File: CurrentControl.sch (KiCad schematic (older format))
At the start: 7 parts

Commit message: Initial Annotation
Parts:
- gave numbers to parts that had none: 7
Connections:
- net at R402.2: now also U201.7; no longer U201.1
- net at Q401.S, R403.1: now also U201.6 (-); no longer U201.2 (-)
- net at R401.1, RV401.3: now also U201.5 (+); no longer U201.3 (+)
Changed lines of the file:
@@
 $EndDescr
 $Comp
-L LMV358 U?
-U 1 1 54DADC5E
+L LMV358 U201
+U 2 1 54DADC5E
 P 5500 3700
-F 0 "U?" H 5450 3900 60  0000 L CNN
+F 0 "U201" H 5450 3900 60  0000 L CNN
 F 1 "LMV358" H 5450 3450 60  0000 L CNN
 F 2 "" H 5500 3700 60  0000 C CNN
 F 3 "" H 5500 3700 60  0000 C CNN
-	1    5500 3700
+	2    5500 3700
 	1    0    0    -1
 $EndComp
 $Comp
-L R R?
+L R R403
 U 1 1 54DADC66
 P 8100 5150
-F 0 "R?" V 8180 5150 50  0000 C CNN
+F 0 "R403" V 8180 5150 50  0000 C CNN
 F 1 ".1" V 8107 5151 50  0000 C CNN
 F 2 "" V 8030 5150 30  0000 C CNN
@@
 $EndComp
 $Comp
-L MOSFET_N Q?
+L MOSFET_N Q401
 U 1 1 54DADC74
 P 8000 3700
-F 0 "Q?" H 8010 3870 50  0000 R CNN
+F 0 "Q401" H 8010 3870 50  0000 R CNN
 F 1 "BUK9575" H 7950 3550 50  0000 R CNN
 F 2 "" H 8000 3700 60  0000 C CNN
@@
 $EndComp
 $Comp
-L R R?
+L R R401
 U 1 1 54DADC7B
 P 3600 4900
-F 0 "R?" V 3680 4900 50  0000 C CNN
+F 0 "R401" V 3680 4900 50  0000 C CNN
 F 1 "R" V 3607 4901 50  0000 C CNN
 F 2 "" V 3530 4900 30  0000 C CNN
@@
 $EndComp
 $Comp
-L GND #PWR?
+L GND #PWR402
 U 1 1 54DADC82
 P 5400 4250
-F 0 "#PWR?" H 5400 4000 60  0001 C CNN
+F 0 "#PWR402" H 5400 4000 60  0001 C CNN
 F 1 "GND" H 5400 4100 60  0000 C CNN
 F 2 "" H 5400 4250 60  0000 C CNN
@@
 Connection ~ 8100 5450
 $Comp
-L POT RV?
+L POT RV401
 U 1 1 54DADC9B
 P 3600 4200
-F 0 "RV?" H 3600 4100 50  0000 C CNN
+F 0 "RV401" H 3600 4100 50  0000 C CNN
 F 1 "POT" H 3600 4200 50  0000 C CNN
 F 2 "" H 3600 4200 60  0000 C CNN
@@
 Connection ~ 3750 2600
 $Comp
-L GND #PWR?
+L GND #PWR401
 U 1 1 54DADCA8
 P 4800 3300
-F 0 "#PWR?" H 4800 3050 60  0001 C CNN
+F 0 "#PWR401" H 4800 3050 60  0001 C CNN
 F 1 "GND" H 4800 3150 60  0000 C CNN
 F 2 "" H 4800 3300 60  0000 C CNN
@@
 $EndComp
 $Comp
-L C C?
+L C C401
 U 1 1 54DADCAE
 P 4800 3050
-F 0 "C?" H 4850 3150 50  0000 L CNN
+F 0 "C401" H 4850 3150 50  0000 L CNN
 F 1 "C" H 4850 2950 50  0000 L CNN
 F 2 "" H 4838 2900 30  0000 C CNN
@@
 	8650 1500 8100 1500
 $Comp
-L R R?
+L R R402
 U 1 1 54DAE31B
 P 6450 3700
-F 0 "R?" V 6530 3700 50  0000 C CNN
+F 0 "R402" V 6530 3700 50  0000 C CNN
 F 1 "1K" V 6457 3701 50  0000 C CNN
 F 2 "" V 6380 3700 30  0000 C CNN

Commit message: Preliminary association of components and placement into layout.
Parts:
- C401, R401, R402: footprint (none) -> SMD_Packages:SMD-0805
- Q401: footprint (none) -> Transistors_TO-220:TO-220_FET-GDS_Vertical
- R403: footprint (none) -> Resistors_ThroughHole:Resistor_Horizontal_RM15mm
- RV401: footprint (none) -> Potentiometers:Potentiometer_WirePads_largePads
- U201: footprint (none) -> SMD_Packages:SOIC-8-N
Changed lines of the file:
@@
 F 0 "U201" H 5450 3900 60  0000 L CNN
 F 1 "LMV358" H 5450 3450 60  0000 L CNN
-F 2 "" H 5500 3700 60  0000 C CNN
+F 2 "SMD_Packages:SOIC-8-N" H 5500 3700 60  0001 C CNN
 F 3 "" H 5500 3700 60  0000 C CNN
 	2    5500 3700
@@
 F 0 "R403" V 8180 5150 50  0000 C CNN
 F 1 ".1" V 8107 5151 50  0000 C CNN
-F 2 "" V 8030 5150 30  0000 C CNN
+F 2 "Resistors_ThroughHole:Resistor_Horizontal_RM15mm" V 8030 5150 30  0001 C CNN
 F 3 "" H 8100 5150 30  0000 C CNN
 F 4 "AC01000001007JA100" V 8100 5150 60  0001 C CNN "MPN"
@@
 F 0 "Q401" H 8010 3870 50  0000 R CNN
 F 1 "BUK9575" H 7950 3550 50  0000 R CNN
-F 2 "" H 8000 3700 60  0000 C CNN
+F 2 "Transistors_TO-220:TO-220_FET-GDS_Vertical" H 8000 3700 60  0001 C CNN
 F 3 "" H 8000 3700 60  0000 C CNN
 F 4 "BUK9575-100A,127" H 8000 3700 60  0001 C CNN "MPN"
@@
 F 0 "R401" V 3680 4900 50  0000 C CNN
 F 1 "R" V 3607 4901 50  0000 C CNN
-F 2 "" V 3530 4900 30  0000 C CNN
+F 2 "SMD_Packages:SMD-0805" V 3530 4900 30  0001 C CNN
 F 3 "" H 3600 4900 30  0000 C CNN
 	1    3600 4900
@@
 $EndComp
 $Comp
-L GND #PWR402
+L GND #PWR06
 U 1 1 54DADC82
 P 5400 4250
-F 0 "#PWR402" H 5400 4000 60  0001 C CNN
+F 0 "#PWR06" H 5400 4000 60  0001 C CNN
 F 1 "GND" H 5400 4100 60  0000 C CNN
 F 2 "" H 5400 4250 60  0000 C CNN
@@
 F 0 "RV401" H 3600 4100 50  0000 C CNN
 F 1 "POT" H 3600 4200 50  0000 C CNN
-F 2 "" H 3600 4200 60  0000 C CNN
+F 2 "Potentiometers:Potentiometer_WirePads_largePads" H 3600 4200 60  0001 C CNN
 F 3 "" H 3600 4200 60  0000 C CNN
 	1    3600 4200
@@
 Connection ~ 3750 2600
 $Comp
-L GND #PWR401
+L GND #PWR07
 U 1 1 54DADCA8
 P 4800 3300
-F 0 "#PWR401" H 4800 3050 60  0001 C CNN
+F 0 "#PWR07" H 4800 3050 60  0001 C CNN
 F 1 "GND" H 4800 3150 60  0000 C CNN
 F 2 "" H 4800 3300 60  0000 C CNN
@@
 F 0 "C401" H 4850 3150 50  0000 L CNN
 F 1 "C" H 4850 2950 50  0000 L CNN
-F 2 "" H 4838 2900 30  0000 C CNN
+F 2 "SMD_Packages:SMD-0805" H 4838 2900 30  0001 C CNN
 F 3 "" H 4800 3050 60  0000 C CNN
 	1    4800 3050
@@
 F 0 "R402" V 6530 3700 50  0000 C CNN
 F 1 "1K" V 6457 3701 50  0000 C CNN
-F 2 "" V 6380 3700 30  0000 C CNN
+F 2 "SMD_Packages:SMD-0805" V 6380 3700 30  0001 C CNN
 F 3 "" H 6450 3700 30  0000 C CNN
 	1    6450 3700

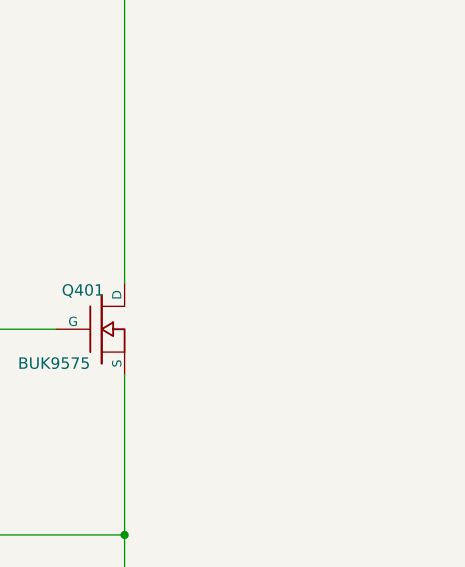
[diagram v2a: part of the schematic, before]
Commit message: Created new footprint library and created a heatsink footprint.
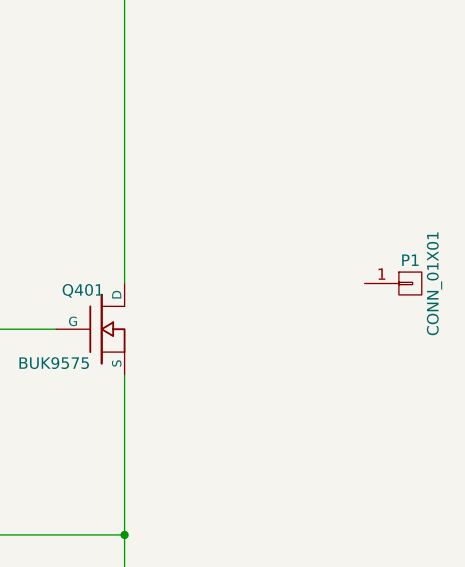
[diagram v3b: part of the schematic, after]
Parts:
- added P1: CONN_01X01, symbol CONN_01X01
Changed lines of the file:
@@
 Text HLabel 8550 6000 2    60   Input ~ 0
 Current_Sink-
+$Comp
+L CONN_01X01 P1
+U 1 1 54DFC527
+P 9350 3500
+F 0 "P1" H 9350 3600 50  0000 C CNN
+F 1 "CONN_01X01" V 9450 3500 50  0000 C CNN
+F 2 "" H 9350 3500 60  0000 C CNN
+F 3 "" H 9350 3500 60  0000 C CNN
+	1    9350 3500
+	1    0    0    -1
+$EndComp
 $EndSCHEMATC

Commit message: Added new potentiometer footprints to layout
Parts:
- P1: footprint (none) -> Current:FA-T220-38E
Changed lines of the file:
@@
 F 0 "P1" H 9350 3600 50  0000 C CNN
 F 1 "CONN_01X01" V 9450 3500 50  0000 C CNN
-F 2 "" H 9350 3500 60  0000 C CNN
+F 2 "Current:FA-T220-38E" H 9350 3500 60  0001 C CNN
 F 3 "" H 9350 3500 60  0000 C CNN
 	1    9350 3500

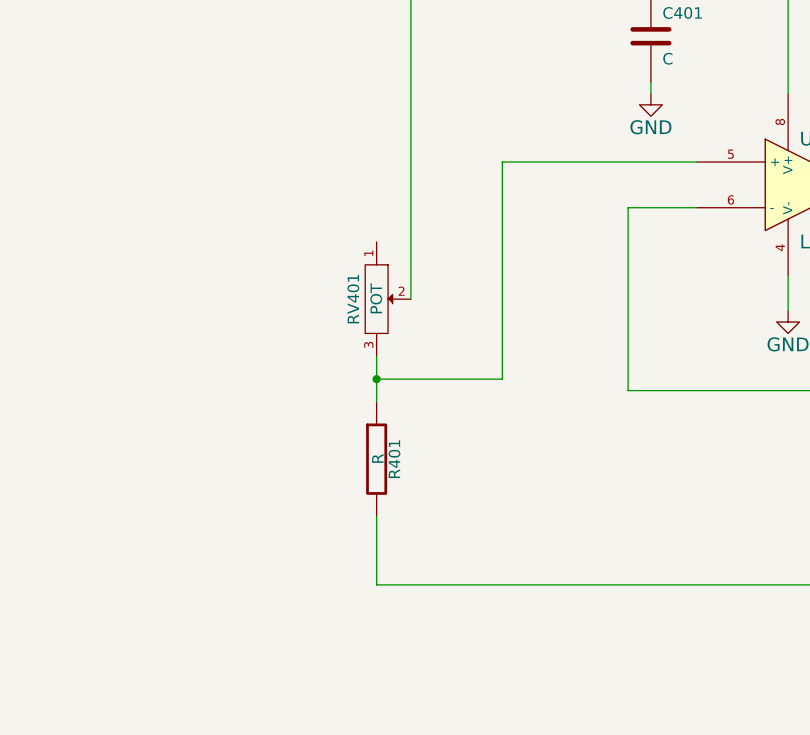
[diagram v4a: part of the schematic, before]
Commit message: Fixed divider resistors and found values
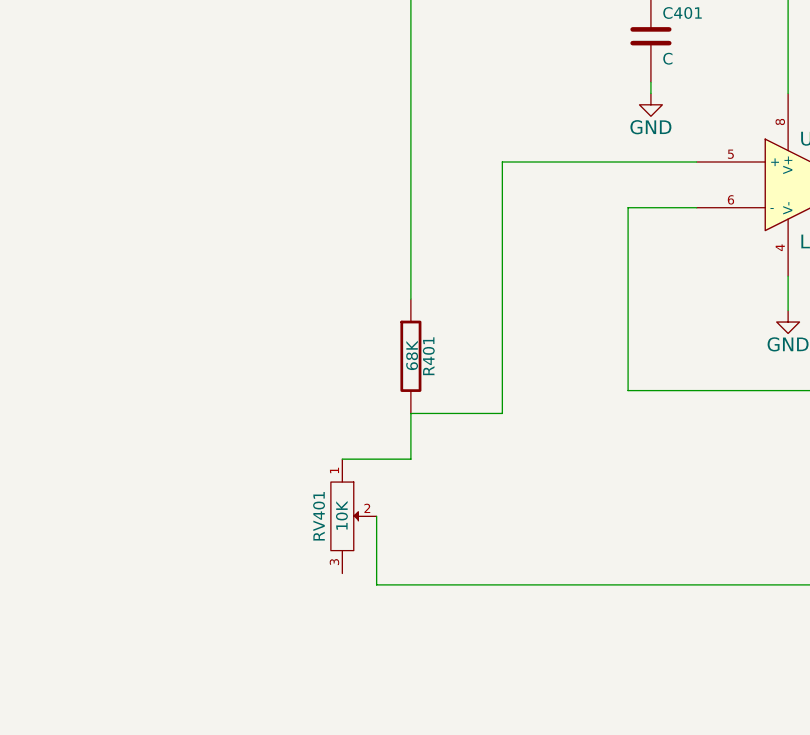
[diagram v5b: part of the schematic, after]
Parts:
- R401: value R -> 68K
- RV401: value POT -> 10K; footprint Potentiometers:Potentiometer_WirePads_largePads -> Current:P090L-02F25BR10K; MPN (none) -> P090L-02F25BR10K
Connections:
- net 2.7V: now also R401.1; no longer RV401.2
- net Current_Sink-: now also RV401.2; no longer R401.2
- net at RV401.1: now also R401.2, U201.5 (+)
- now unconnected: RV401.3
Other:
- moved on the sheet: R401, RV401
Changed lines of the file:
@@
 L R R401
 U 1 1 54DADC7B
-P 3600 4900
-F 0 "R401" V 3680 4900 50  0000 C CNN
-F 1 "R" V 3607 4901 50  0000 C CNN
-F 2 "SMD_Packages:SMD-0805" V 3530 4900 30  0001 C CNN
-F 3 "" H 3600 4900 30  0000 C CNN
-	1    3600 4900
+P 3750 4450
+F 0 "R401" V 3830 4450 50  0000 C CNN
+F 1 "68K" V 3757 4451 50  0000 C CNN
+F 2 "SMD_Packages:SMD-0805" V 3680 4450 30  0001 C CNN
+F 3 "" H 3750 4450 30  0000 C CNN
+	1    3750 4450
 	1    0    0    -1
 $EndComp
@@
 	5000 3600 4150 3600
 Wire Wire Line
-	4150 3600 4150 4550
-Wire Wire Line
-	4150 4550 3600 4550
-Wire Wire Line
-	3600 4450 3600 4650
-Connection ~ 3600 4550
+	4150 3600 4150 4700
 Wire Wire Line
 	3600 5150 3600 5450
@@
 L POT RV401
 U 1 1 54DADC9B
-P 3600 4200
-F 0 "RV401" H 3600 4100 50  0000 C CNN
-F 1 "POT" H 3600 4200 50  0000 C CNN
-F 2 "Potentiometers:Potentiometer_WirePads_largePads" H 3600 4200 60  0001 C CNN
-F 3 "" H 3600 4200 60  0000 C CNN
-	1    3600 4200
+P 3450 5150
+F 0 "RV401" H 3450 5050 50  0000 C CNN
+F 1 "10K" H 3450 5150 50  0000 C CNN
+F 2 "Current:P090L-02F25BR10K" H 3450 5150 60  0001 C CNN
+F 3 "" H 3450 5150 60  0000 C CNN
+F 4 "P090L-02F25BR10K" H 3450 5150 60  0001 C CNN "MPN"
+	1    3450 5150
 	0    1    1    0
 $EndComp
@@
 	1    0    0    -1
 $EndComp
+Wire Wire Line
+	4150 4700 3750 4700
+Wire Wire Line
+	3750 4700 3750 4900
+Wire Wire Line
+	3750 4900 3450 4900
 $EndSCHEMATC

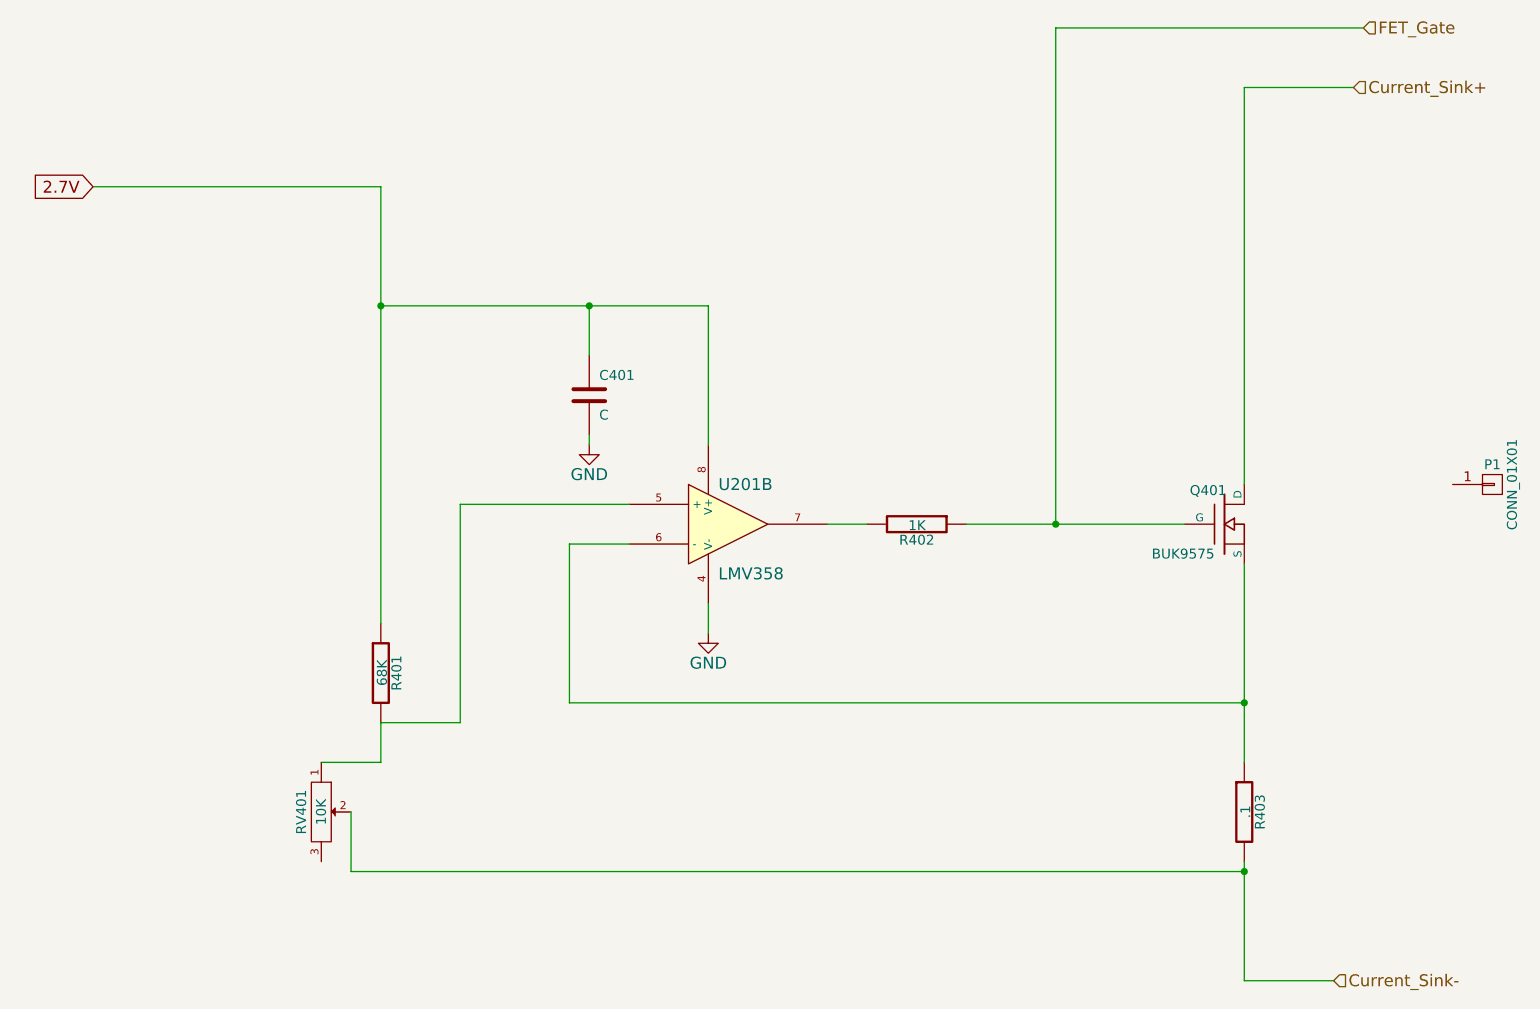
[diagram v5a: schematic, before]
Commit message: Cosmetic cleanup of schematic
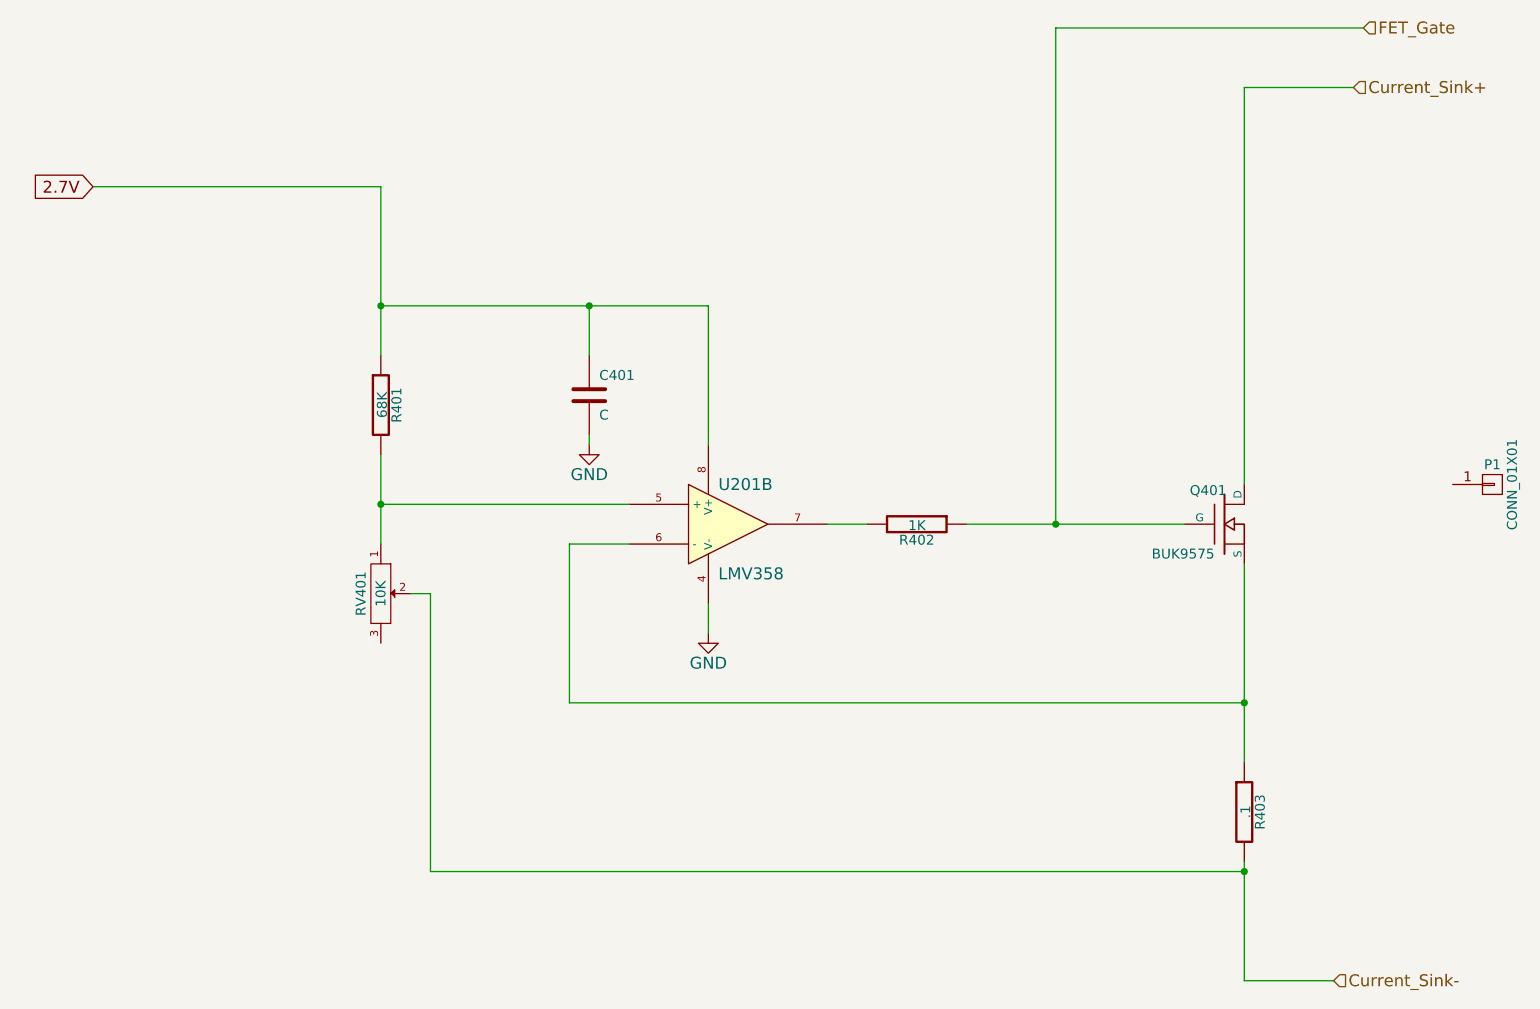
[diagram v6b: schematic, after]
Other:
- moved on the sheet: R401, RV401
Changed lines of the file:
@@
-$EndComp
-$Comp
-L R R401
-U 1 1 54DADC7B
-P 3750 4450
-F 0 "R401" V 3830 4450 50  0000 C CNN
-F 1 "68K" V 3757 4451 50  0000 C CNN
-F 2 "SMD_Packages:SMD-0805" V 3680 4450 30  0001 C CNN
-F 3 "" H 3750 4450 30  0000 C CNN
-	1    3750 4450
-	1    0    0    -1
 $EndComp
 $Comp
@@
 Connection ~ 8100 4600
 Wire Wire Line
-	5000 3600 4150 3600
-Wire Wire Line
-	4150 3600 4150 4700
-Wire Wire Line
-	3600 5150 3600 5450
-Wire Wire Line
-	3600 5450 8100 5450
+	3750 3600 5000 3600
 Connection ~ 8100 5450
 $Comp
 L POT RV401
 U 1 1 54DADC9B
-P 3450 5150
-F 0 "RV401" H 3450 5050 50  0000 C CNN
-F 1 "10K" H 3450 5150 50  0000 C CNN
-F 2 "Current:P090L-02F25BR10K" H 3450 5150 60  0001 C CNN
-F 3 "" H 3450 5150 60  0000 C CNN
-F 4 "P090L-02F25BR10K" H 3450 5150 60  0001 C CNN "MPN"
-	1    3450 5150
+P 3750 4050
+F 0 "RV401" H 3750 3950 50  0000 C CNN
+F 1 "10K" H 3750 4050 50  0000 C CNN
+F 2 "Current:P090L-02F25BR10K" H 3750 4050 60  0001 C CNN
+F 3 "" H 3750 4050 60  0000 C CNN
+F 4 "P090L-02F25BR10K" H 3750 4050 60  0001 C CNN "MPN"
+	1    3750 4050
 	0    1    1    0
 $EndComp
@@
 	2300 2000 3750 2000
 Wire Wire Line
-	3750 2000 3750 4200
+	3750 2000 3750 2850
 Text HLabel 8650 1500 2    60   Input ~ 0
 Current_Sink+
@@
 	1    0    0    -1
 $EndComp
+$Comp
+L R R401
+U 1 1 54DADC7B
+P 3750 3100
+F 0 "R401" V 3830 3100 50  0000 C CNN
+F 1 "68K" V 3757 3101 50  0000 C CNN
+F 2 "SMD_Packages:SMD-0805" V 3680 3100 30  0001 C CNN
+F 3 "" H 3750 3100 30  0000 C CNN
+	1    3750 3100
+	1    0    0    -1
+$EndComp
 Wire Wire Line
-	4150 4700 3750 4700
+	3750 3350 3750 3800
+Connection ~ 3750 3600
 Wire Wire Line
-	3750 4700 3750 4900
+	3900 4050 4000 4050
 Wire Wire Line
-	3750 4900 3450 4900
+	4000 4050 4000 5450
+Wire Wire Line
+	4000 5450 8100 5450
 $EndSCHEMATC

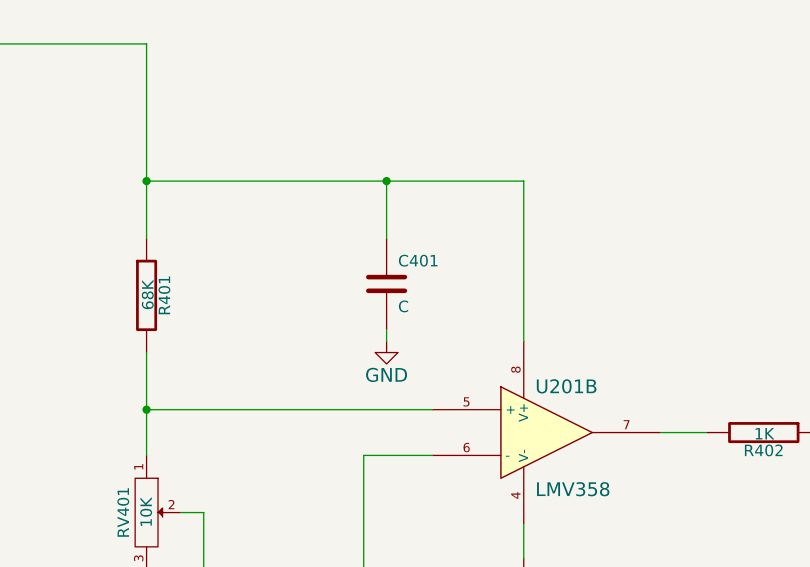
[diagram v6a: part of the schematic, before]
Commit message: Moved pots/terms and routed traces to all components
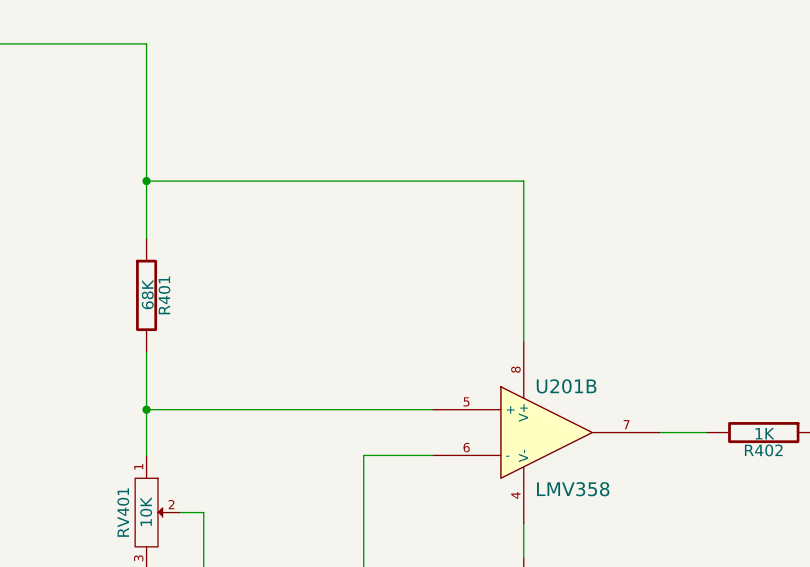
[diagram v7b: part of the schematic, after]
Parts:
- removed C401: C, SMD_Packages:SMD-0805, symbol C
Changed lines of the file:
@@
 	5400 2600 5400 3300
 Connection ~ 3750 2600
-$Comp
-L GND #PWR07
-U 1 1 54DADCA8
-P 4800 3300
-F 0 "#PWR07" H 4800 3050 60  0001 C CNN
-F 1 "GND" H 4800 3150 60  0000 C CNN
-F 2 "" H 4800 3300 60  0000 C CNN
-F 3 "" H 4800 3300 60  0000 C CNN
-	1    4800 3300
-	1    0    0    -1
-$EndComp
-$Comp
-L C C401
-U 1 1 54DADCAE
-P 4800 3050
-F 0 "C401" H 4850 3150 50  0000 L CNN
-F 1 "C" H 4850 2950 50  0000 L CNN
-F 2 "SMD_Packages:SMD-0805" H 4838 2900 30  0001 C CNN
-F 3 "" H 4800 3050 60  0000 C CNN
-	1    4800 3050
-	1    0    0    -1
-$EndComp
-Wire Wire Line
-	4800 2850 4800 2600
-Connection ~ 4800 2600
-Wire Wire Line
-	4800 3300 4800 3250
 Wire Wire Line
 	8100 1500 8100 3500
